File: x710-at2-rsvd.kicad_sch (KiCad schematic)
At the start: 37 parts, among them J7 PinHeader_1x3_P2.54mm_Drill1.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, U4 EZX710AT2_S_LMR5

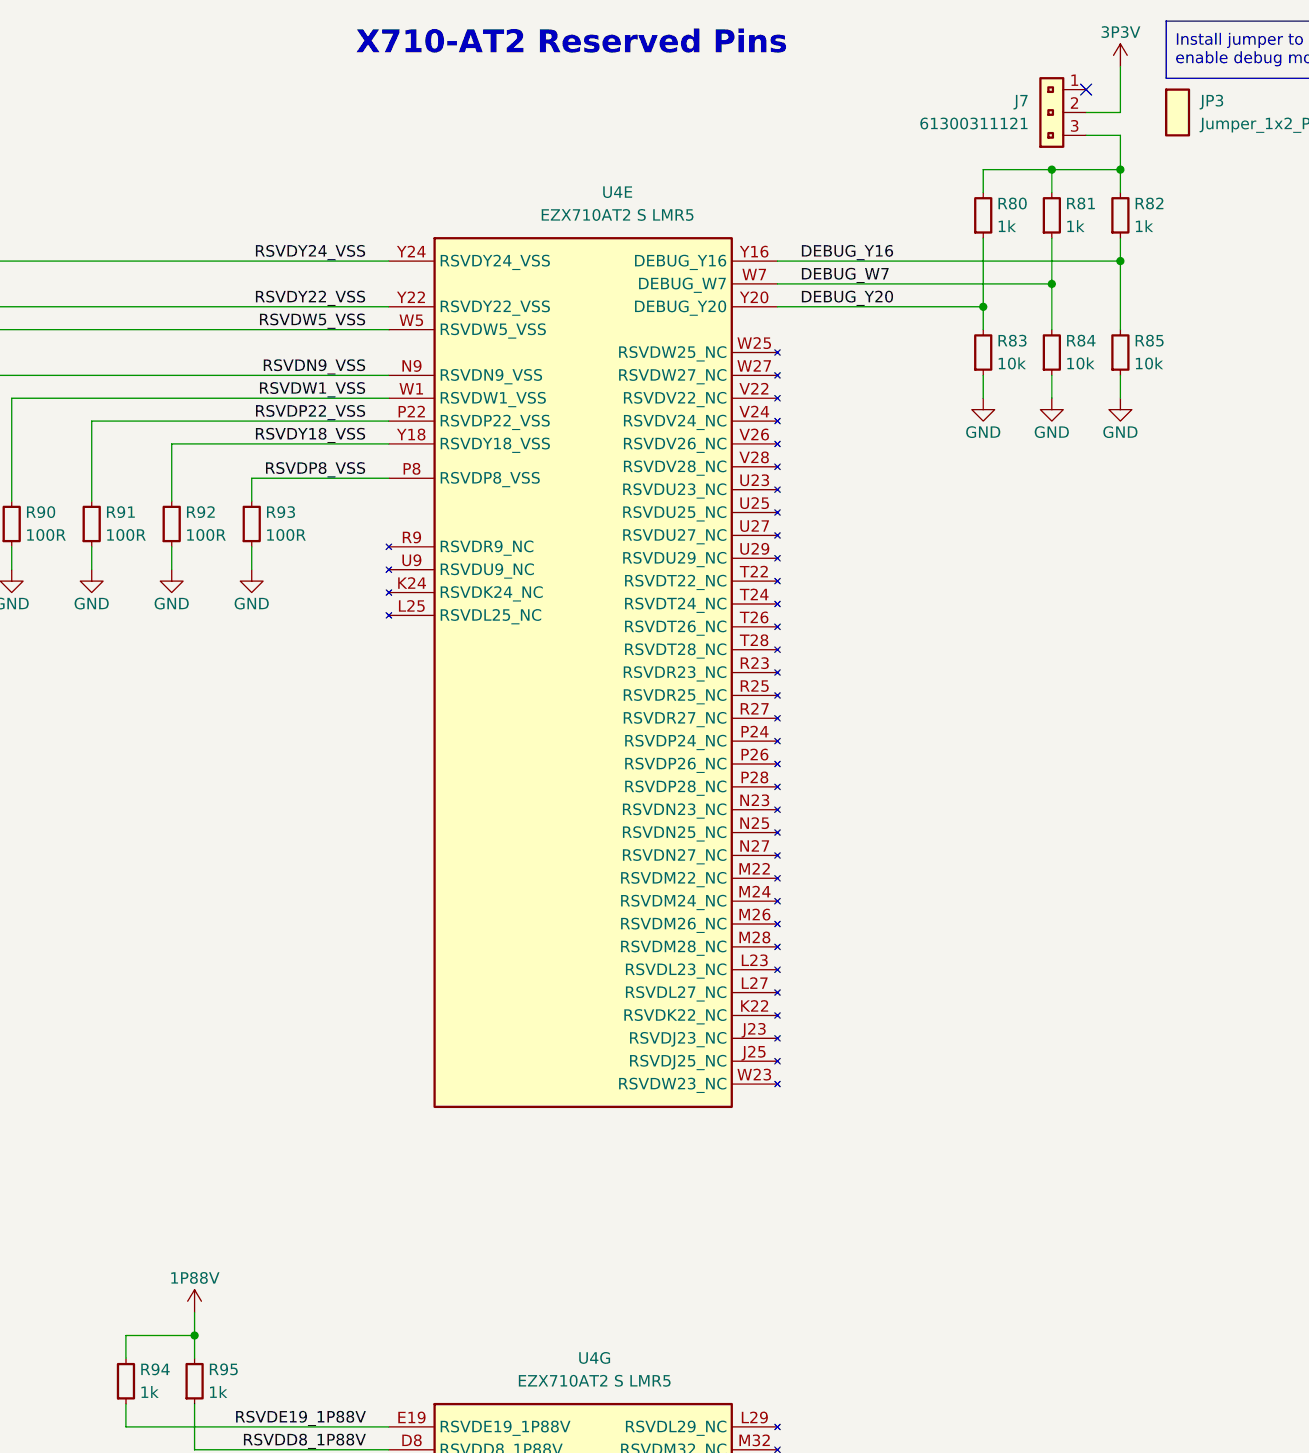
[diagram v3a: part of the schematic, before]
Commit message: [#80813] Change 3V3 and 1V88 power rails names
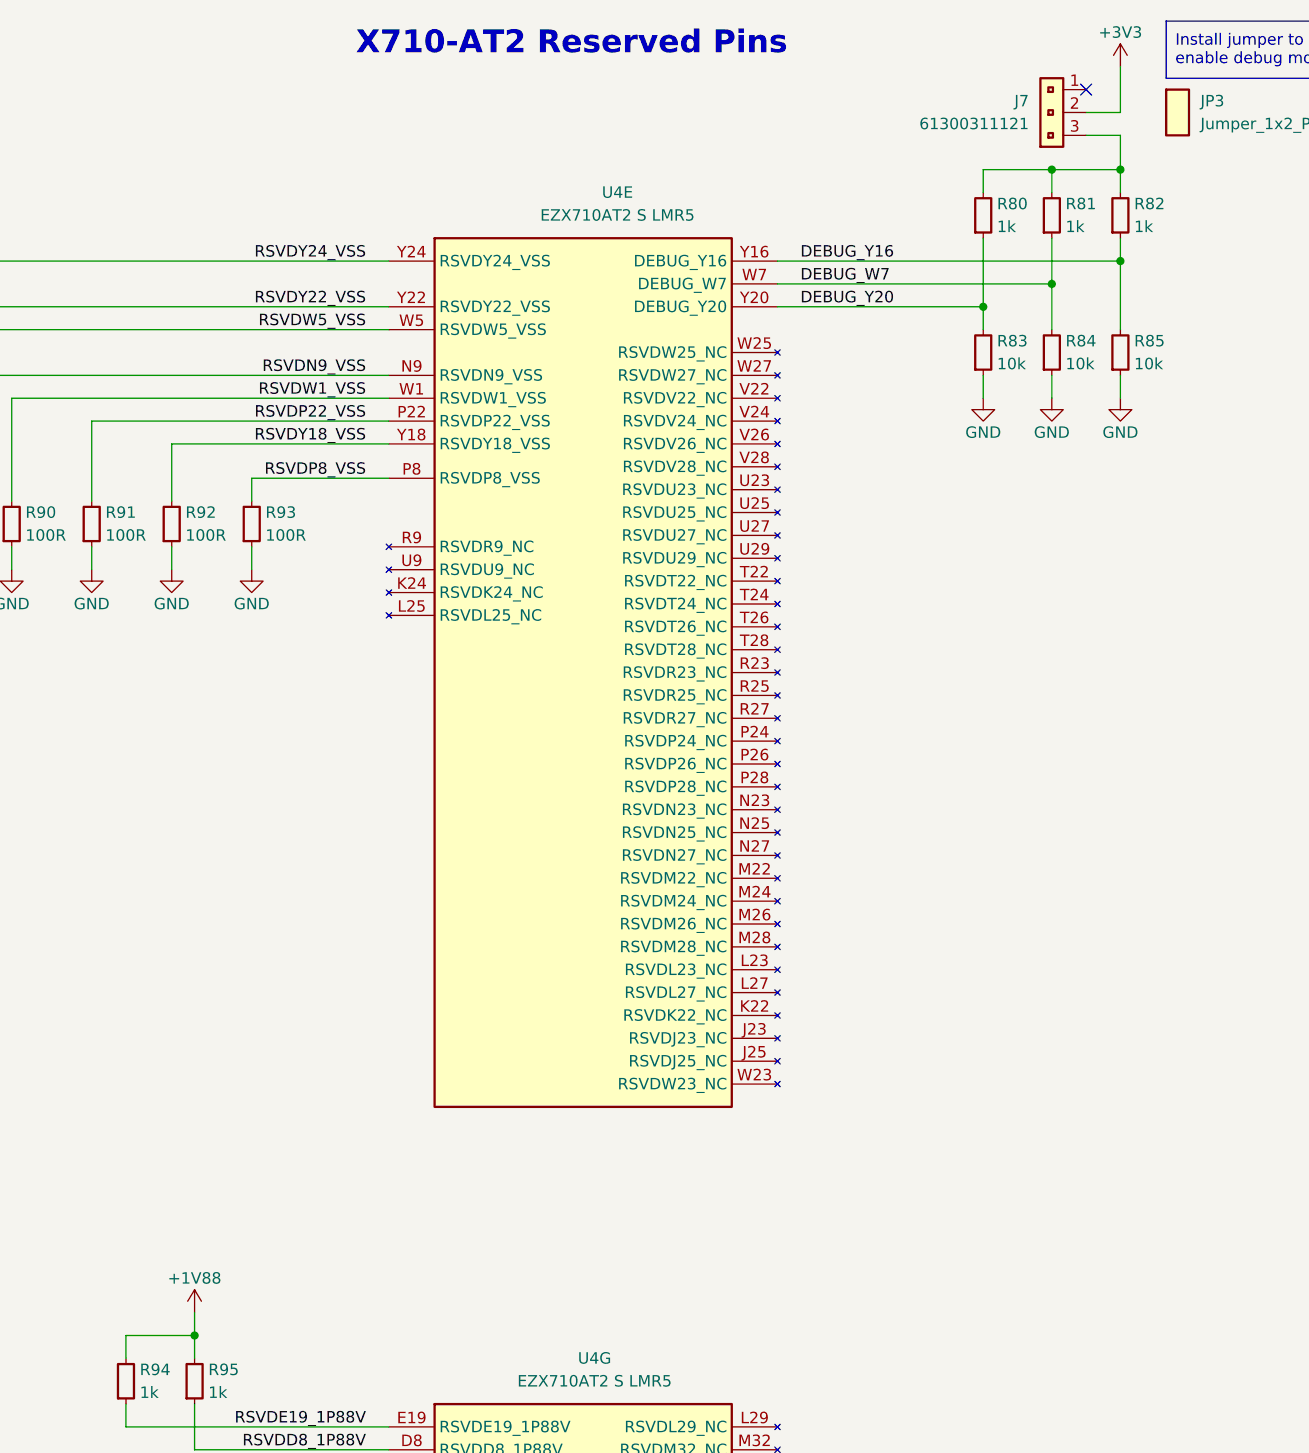
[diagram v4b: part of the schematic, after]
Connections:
- net 1P88V renamed +1V88
- net 3P3V renamed +3V3
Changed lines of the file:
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@@
+	)
+	(symbol
+		(lib_id "antmicropower:+1V8")
+		(at 173.99 166.37 0)
+		(unit 1)
+		(exclude_from_sim no)
+		(in_bom yes)
+		(on_board yes)
+		(dnp no)
+		(property "Reference" "#PWR094"
+			(at 189.23 168.91 0)
+			(effects
+				(font
+					(size 1.27 1.27)
+					(thickness 0.15)
+				)
+				(justify left bottom)
+				(hide yes)
+			)
+		)
+		(property "Value" "+1V88"
+			(at 173.99 162.56 0)
+			(effects
+				(font
+					(size 1.27 1.27)
+					(thickness 0.15)
+				)
+			)
+		)
+		(property "Footprint" ""
+			(at 189.23 173.99 0)
+			(effects
+				(font
+					(size 1.27 1.27)
+					(thickness 0.15)
+				)
+				(justify left bottom)
+				(hide yes)
+			)
+		)
+		(property "Datasheet" ""
+			(at 189.23 176.53 0)
+			(effects
+				(font
+					(size 1.27 1.27)
+					(thickness 0.15)
+				)
+				(justify left bottom)
+				(hide yes)
+			)
+		)
+		(property "Description" ""
+			(at 173.99 166.37 0)
+			(effects
+				(font
+					(size 1.27 1.27)
+				)
+				(hide yes)
+			)
+		)
+		(property "Author" "Antmicro"
+			(at 189.23 171.45 0)
+			(effects
+				(font
+					(size 1.27 1.27)
+					(thickness 0.15)
+				)
+				(justify left bottom)
+				(hide yes)
+			)
+		)
+		(property "License" "Apache-2.0"
+			(at 189.23 173.99 0)
+			(effects
+				(font
+					(size 1.27 1.27)
+					(thickness 0.15)
+				)
+				(justify left bottom)
+				(hide yes)
+			)
+		)
+		(pin "1"
+		)
+		(instances
+			(project "10-gbe-expansion"
+				(path "/04bda987-e5eb-48b4-9e90-d8211dc11b39/5c16e05d-0fb9-4db6-bb95-cf7113880df7"
+					(reference "#PWR094")
+					(unit 1)
+				)
+			)
+		)
 	)
 	(symbol
@@
 	)
 	(symbol
+		(lib_id "antmicropower:+3V3")
+		(at 276.86 27.94 0)
+		(unit 1)
+		(exclude_from_sim no)
+		(in_bom yes)
+		(on_board yes)
+		(dnp no)
+		(property "Reference" "#PWR081"
+			(at 292.1 27.94 0)
+			(effects
+				(font
+					(size 1.27 1.27)
+					(thickness 0.15)
+				)
+				(justify left bottom)
+				(hide yes)
+			)
+		)
+		(property "Value" "+3V3"
+			(at 276.86 24.13 0)
+			(effects
+				(font
+					(size 1.27 1.27)
+					(thickness 0.15)
+				)
+			)
+		)
+		(property "Footprint" ""
+			(at 292.1 35.56 0)
+			(effects
+				(font
+					(size 1.27 1.27)
+					(thickness 0.15)
+				)
+				(justify left bottom)
+				(hide yes)
+			)
+		)
+		(property "Datasheet" ""
+			(at 292.1 38.1 0)
+			(effects
+				(font
+					(size 1.27 1.27)
+					(thickness 0.15)
+				)
+				(justify left bottom)
+				(hide yes)
+			)
+		)
+		(property "Description" ""
+			(at 276.86 27.94 0)
+			(effects
+				(font
+					(size 1.27 1.27)
+				)
+				(hide yes)
+			)
+		)
+		(property "Author" "Antmicro"
+			(at 292.1 30.48 0)
+			(effects
+				(font
+					(size 1.27 1.27)
+					(thickness 0.15)
+				)
+				(justify left bottom)
+				(hide yes)
+			)
+		)
+		(property "License" "Apache-2.0"
+			(at 292.1 33.02 0)
+			(effects
+				(font
+					(size 1.27 1.27)
+					(thickness 0.15)
+				)
+				(justify left bottom)
+				(hide yes)
+			)
+		)
+		(pin "1"
+		)
+		(instances
+			(project "10-gbe-expansion"
+				(path "/04bda987-e5eb-48b4-9e90-d8211dc11b39/5c16e05d-0fb9-4db6-bb95-cf7113880df7"
+					(reference "#PWR081")
+					(unit 1)
+				)
+			)
+		)
+	)
+	(symbol
 		(lib_id "antmicroResistors0402:R_0R_0402")
 		(at 100.33 247.65 90)
@@
 				(path "/04bda987-e5eb-48b4-9e90-d8211dc11b39/5c16e05d-0fb9-4db6-bb95-cf7113880df7"
 					(reference "R103")
-					(unit 1)
-				)
-			)
-		)
-	)
-	(symbol
-		(lib_id "antmicropower:VCC")
-		(at 276.86 27.94 0)
-		(unit 1)
-		(exclude_from_sim no)
-		(in_bom yes)
-		(on_board yes)
-		(dnp no)
-		(property "Reference" "#PWR081"
-			(at 276.86 31.75 0)
-			(effects
-				(font
-					(size 1.27 1.27)
-				)
-				(hide yes)
-			)
-		)
-		(property "Value" "3P3V"
-			(at 276.86 24.13 0)
-			(effects
-				(font
-					(size 1.27 1.27)
-				)
-			)
-		)
-		(property "Footprint" ""
-			(at 276.86 27.94 0)
-			(effects
-				(font
-					(size 1.27 1.27)
-				)
-				(hide yes)
-			)
-		)
-		(property "Datasheet" ""
-			(at 276.86 27.94 0)
-			(effects
-				(font
-					(size 1.27 1.27)
-				)
-				(hide yes)
-			)
-		)
-		(property "Description" ""
-			(at 276.86 27.94 0)
-			(effects
-				(font
-					(size 1.27 1.27)
-				)
-				(hide yes)
-			)
-		)
-		(pin "1"
-		)
-		(instances
-			(project "10-gbe-expansion"
-				(path "/04bda987-e5eb-48b4-9e90-d8211dc11b39/5c16e05d-0fb9-4db6-bb95-cf7113880df7"
-					(reference "#PWR081")
 					(unit 1)
 				)
@@
 					(unit 1)
 				)
-			)
-		)
-	)
-	(symbol
-		(lib_id "antmicropower:VDD")
-		(at 173.99 166.37 0)
-		(unit 1)
-		(exclude_from_sim no)
-		(in_bom yes)
-		(on_board yes)
-		(dnp no)
-		(property "Reference" "#PWR094"
-			(at 173.99 170.18 0)
-			(effects
-				(font
-					(size 1.27 1.27)
-				)
-				(hide yes)
-			)
-		)
-		(property "Value" "1P88V"
-			(at 173.99 162.56 0)
-			(effects
-				(font
-					(size 1.27 1.27)
-				)
-			)
-		)
-		(property "Footprint" ""
-			(at 173.99 166.37 0)
-			(effects
-				(font
-					(size 1.27 1.27)
-				)
-				(hide yes)
-			)
-		)
-		(property "Datasheet" ""
-			(at 173.99 166.37 0)
-			(effects
-				(font
-					(size 1.27 1.27)
-				)
-				(hide yes)
-			)
-		)
-		(property "Description" ""
-			(at 173.99 166.37 0)
-			(effects
-				(font
-					(size 1.27 1.27)
-				)
-				(hide yes)
-			)
-		)
-		(pin "1"
-		)
-		(instances
-			(project "10-gbe-expansion"
-				(path "/04bda987-e5eb-48b4-9e90-d8211dc11b39/5c16e05d-0fb9-4db6-bb95-cf7113880df7"
-					(reference "#PWR094")
-					(unit 1)
-				)

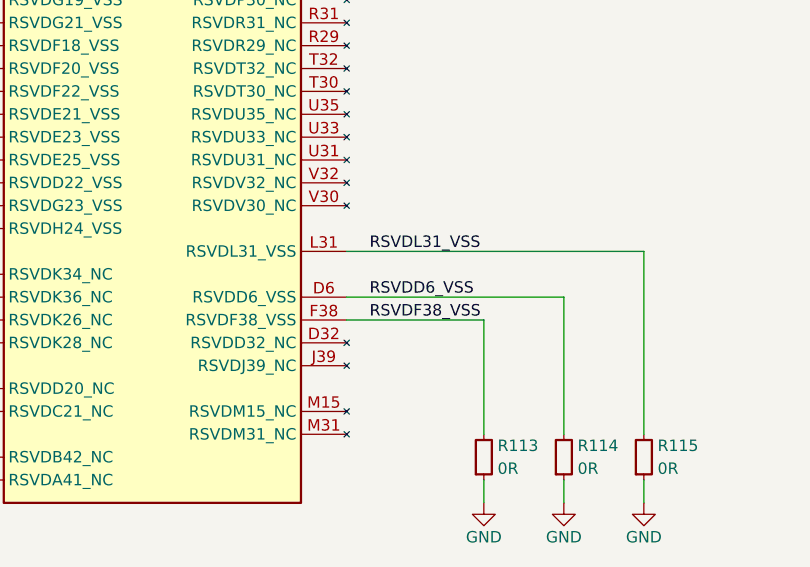
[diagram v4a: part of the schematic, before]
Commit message: [#80813] WIP: Adjust passives values, add missing load capacitors for the 50MHz resonator
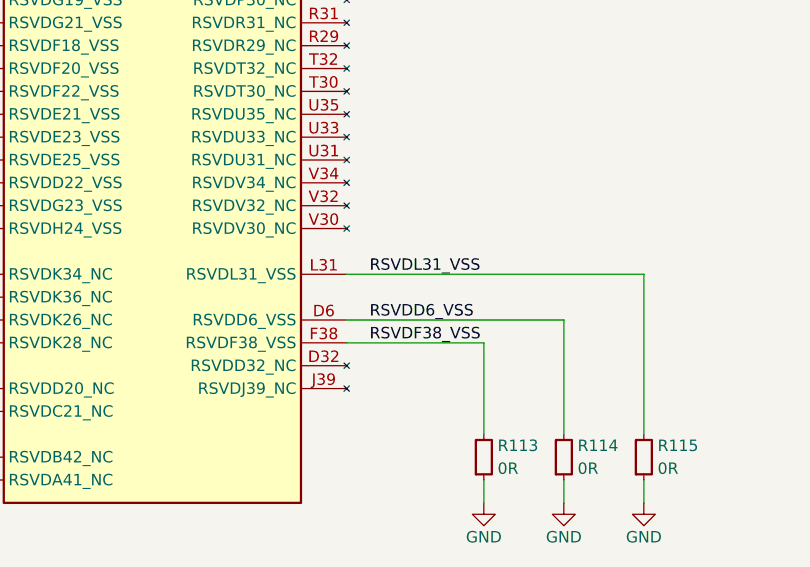
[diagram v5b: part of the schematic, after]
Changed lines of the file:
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@@
 	(wire
 		(pts
+			(xy 271.78 247.65) (xy 271.78 250.19)
+		)
+		(stroke
+			(width 0)
+			(type default)
+		)
+	)
+	(wire
+		(pts
 			(xy 273.05 33.02) (xy 276.86 33.02)
 		)
@@
 	(wire
 		(pts
-			(xy 118.11 247.65) (xy 118.11 250.19)
+			(xy 262.89 247.65) (xy 262.89 250.19)
 		)
 		(stroke
@@
 	(wire
 		(pts
-			(xy 269.24 39.37) (xy 276.86 39.37)
+			(xy 118.11 247.65) (xy 118.11 250.19)
 		)
 		(stroke
@@
 	(wire
 		(pts
-			(xy 254 247.65) (xy 254 250.19)
+			(xy 269.24 39.37) (xy 276.86 39.37)
 		)
 		(stroke
@@
 	(wire
 		(pts
-			(xy 254 229.87) (xy 254 242.57)
+			(xy 262.89 229.87) (xy 262.89 242.57)
 		)
 		(stroke
@@
 	(wire
 		(pts
-			(xy 262.89 227.33) (xy 262.89 242.57)
+			(xy 55.88 184.15) (xy 195.58 184.15)
 		)
 		(stroke
@@
 	(wire
 		(pts
-			(xy 55.88 184.15) (xy 195.58 184.15)
+			(xy 238.76 224.79) (xy 271.78 224.79)
 		)
 		(stroke
@@
 	(wire
 		(pts
-			(xy 271.78 247.65) (xy 271.78 250.19)
-		)
-		(stroke
-			(width 0)
-			(type default)
-		)
-	)
-	(wire
-		(pts
-			(xy 271.78 242.57) (xy 271.78 222.25)
+			(xy 238.76 232.41) (xy 254 232.41)
 		)
 		(stroke
@@
 	(wire
 		(pts
-			(xy 238.76 227.33) (xy 262.89 227.33)
-		)
-		(stroke
-			(width 0)
-			(type default)
-		)
-	)
-	(wire
-		(pts
-			(xy 238.76 229.87) (xy 254 229.87)
-		)
-		(stroke
-			(width 0)
-			(type default)
-		)
-	)
-	(wire
-		(pts
 			(xy 171.45 247.65) (xy 171.45 250.19)
 		)
@@
 	(wire
 		(pts
-			(xy 238.76 222.25) (xy 271.78 222.25)
-		)
-		(stroke
-			(width 0)
-			(type default)
-		)
-	)
-	(wire
-		(pts
 			(xy 162.56 67.31) (xy 195.58 67.31)
 		)
@@
 	(wire
 		(pts
+			(xy 238.76 229.87) (xy 262.89 229.87)
+		)
+		(stroke
+			(width 0)
+			(type default)
+		)
+	)
+	(wire
+		(pts
 			(xy 73.66 189.23) (xy 195.58 189.23)
 		)
@@
 	(wire
 		(pts
-			(xy 153.67 76.2) (xy 153.67 64.77)
+			(xy 254 247.65) (xy 254 250.19)
 		)
 		(stroke
@@
 	(wire
 		(pts
-			(xy 269.24 41.91) (xy 269.24 39.37)
+			(xy 153.67 76.2) (xy 153.67 64.77)
 		)
 		(stroke
@@
 	(wire
 		(pts
-			(xy 109.22 199.39) (xy 195.58 199.39)
+			(xy 269.24 41.91) (xy 269.24 39.37)
 		)
 		(stroke
@@
 	(wire
 		(pts
-			(xy 171.45 69.85) (xy 195.58 69.85)
+			(xy 109.22 199.39) (xy 195.58 199.39)
 		)
 		(stroke
@@
 	(wire
 		(pts
-			(xy 262.89 247.65) (xy 262.89 250.19)
+			(xy 171.45 69.85) (xy 195.58 69.85)
 		)
 		(stroke
@@
 	(wire
 		(pts
+			(xy 254 232.41) (xy 254 242.57)
+		)
+		(stroke
+			(width 0)
+			(type default)
+		)
+	)
+	(wire
+		(pts
 			(xy 118.11 201.93) (xy 195.58 201.93)
 		)
@@
 	(wire
 		(pts
+			(xy 271.78 242.57) (xy 271.78 224.79)
+		)
+		(stroke
+			(width 0)
+			(type default)
+		)
+	)
+	(wire
+		(pts
 			(xy 276.86 49.53) (xy 276.86 57.15)
 		)
@@
 		)
 	)
-	(label "RSVDL31_VSS"
-		(at 241.3 222.25 0)
-		(effects
-			(font
-				(size 1.27 1.27)
-			)
-			(justify left bottom)
-		)
-	)
 	(label "RSVDH22_VSS"
 		(at 193.04 191.77 180)
@@
 		)
 	)
-	(label "RSVDF38_VSS"
-		(at 241.3 229.87 0)
+	(label "RSVDG21_VSS"
+		(at 193.04 196.85 180)
 		(effects
 			(font
 				(size 1.27 1.27)
 			)
-			(justify left bottom)
+			(justify right bottom)
 		)
 	)
-	(label "RSVDG21_VSS"
-		(at 193.04 196.85 180)
+	(label "RSVDF38_VSS"
+		(at 241.3 232.41 0)
 		(effects
 			(font
 				(size 1.27 1.27)
 			)
-			(justify right bottom)
+			(justify left bottom)
 		)
 	)
@@
 		)
 	)
-	(label "RSVDD6_VSS"
-		(at 241.3 227.33 0)
-		(effects
-			(font
-				(size 1.27 1.27)
-			)
-			(justify left bottom)
-		)
-	)
 	(label "RSVDW1_VSS"
 		(at 193.04 64.77 180)
@@
 		)
 	)
+	(label "RSVDD6_VSS"
+		(at 241.3 229.87 0)
+		(effects
+			(font
+				(size 1.27 1.27)
+			)
+			(justify left bottom)
+		)
+	)
 	(label "RSVDD8_1P88V"
 		(at 193.04 181.61 180)
@@
 		)
 	)
+	(label "RSVDL31_VSS"
+		(at 241.3 224.79 0)
+		(effects
+			(font
+				(size 1.27 1.27)
+			)
+			(justify left bottom)
+		)
+	)
 	(symbol
 		(lib_id "antmicropower:GND")
@@
 		(pin "U37"
 		)
-		(pin "M31"
-		)
 		(pin "AC7"
 		)
@@
 		(pin "J13"
 		)
-		(pin "M15"
-		)
 		(pin "M10"
 		)
@@
 		(pin "Y42"
 		)
+		(pin "V34"
+		)
 		(instances
